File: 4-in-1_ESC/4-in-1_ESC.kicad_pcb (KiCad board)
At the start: 2 copper layers, 223 parts, among them CN1 SM10B-SRSS-TB, CN2 SM07B-SRSS-TB, Q1 BSC070N10NS3G, Q10 BSC070N10NS3G, Q11 BSC070N10NS3G, Q12 BSC070N10NS3G, Q13 BSC070N10NS3G, Q14 BSC070N10NS3G, Q15 BSC070N10NS3G, Q16 BSC070N10NS3G, Q17 BSC070N10NS3G, Q18 BSC070N10NS3G, Q19 BSC070N10NS3G, Q2 BSC070N10NS3G, Q20 BSC070N10NS3G, Q21 BSC070N10NS3G, Q22 BSC070N10NS3G, Q23 BSC070N10NS3G, Q24 BSC070N10NS3G, Q3 BSC070N10NS3G, Q4 BSC070N10NS3G, Q5 BSC070N10NS3G, Q6 BSC070N10NS3G, Q7 BSC070N10NS3G, Q8 BSC070N10NS3G, Q9 BSC070N10NS3G, U1 INA181A2IDBVR, U10 LMR51610XDBVR, U11 AMS1117-3.3_C347222, U12 STM32G071GBU6, U13 STM32G071GBU6, U2 JSM6288Q, U3 JSM6288Q, U4 JSM6288Q, U5 JSM6288Q, U6 STM32G071GBU6, U7 STM32G071GBU6

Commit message: update
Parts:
- removed C25: 100nF, Capacitor_SMD:C_0402_1005Metric
- removed R10, R13, R25, R28, R31, R43, R46, R7: 130k, Resistor_SMD:R_0402_1005Metric
- removed R12, R15, R27, R30, R33, R9: 1k, Resistor_SMD:R_0402_1005Metric
- added C82: 10nF, Capacitor_SMD:C_0201_0603Metric, F.Cu at (76.5, 44.4)
- added C86: 10nF, Capacitor_SMD:C_0201_0603Metric, F.Cu at (76.5, 46.2)
- added D13: XL-0201UGC, LED_SMD:LED_0201_0603Metric, F.Cu at (84.5, 78.6)
- added D14: XL-0201UGC, LED_SMD:LED_0201_0603Metric, F.Cu at (68.2, 122.1)
- added D15: XL-0201UGC, LED_SMD:LED_0201_0603Metric, F.Cu at (64.3, 78.6)
- added D16: XL-0201UGC, LED_SMD:LED_0201_0603Metric, F.Cu at (90.9, 63.0)
- added G***: LOGO, LOGO, F.Cu at (140.0, 105.9)
- added G***: LOGO, LOGO, F.Cu at (147.5, 81.7)
- added H4: MountingHole_Pad, MountingHole:MountingHole_3.2mm_M3_DIN965_Pad_TopBottom, F.Cu at (162.8, 81.7)
- added H5: MountingHole_Pad, MountingHole:MountingHole_3.2mm_M3_DIN965_Pad_TopBottom, F.Cu at (132.2, 81.7)
- added H6: MountingHole_Pad, MountingHole:MountingHole_3.2mm_M3_DIN965_Pad_TopBottom, F.Cu at (162.8, 112.2)
- added H7: MountingHole_Pad, MountingHole:MountingHole_3.2mm_M3_DIN965_Pad_TopBottom, F.Cu at (132.2, 112.2)
- added J1: BLDC Solder Pads, easyeda_import:3_Phase_Solder_Pads, F.Cu at (130.0, 88.4)
- added J2: BLDC Solder Pads, easyeda_import:3_Phase_Solder_Pads, F.Cu at (130.0, 105.3)
- added J3: BLDC Solder Pads, easyeda_import:3_Phase_Solder_Pads, F.Cu at (164.8, 89.8)
- added J4: BLDC Solder Pads, easyeda_import:3_Phase_Solder_Pads, F.Cu at (164.8, 106.4)
- added R100: 100R, Resistor_SMD:R_0201_0603Metric, F.Cu at (78.9, 81.5)
- added R101: 100R, Resistor_SMD:R_0201_0603Metric, F.Cu at (62.6, 124.9)
- added R102: 100R, Resistor_SMD:R_0201_0603Metric, F.Cu at (58.7, 81.5)
- added R103: 100R, Resistor_SMD:R_0201_0603Metric, F.Cu at (85.3, 65.8)
- added R104: 10k, Resistor_SMD:R_0201_0603Metric, F.Cu at (78.9, 83.2)
- added R105: 10k, Resistor_SMD:R_0201_0603Metric, F.Cu at (62.6, 126.7)
- added R106: 10k, Resistor_SMD:R_0201_0603Metric, F.Cu at (58.7, 83.2)
- added R107: 10k, Resistor_SMD:R_0201_0603Metric, F.Cu at (85.3, 67.6)
- added R108: 470R, Resistor_SMD:R_0201_0603Metric, F.Cu at (144.4, 120.4)
- added R109: 470R, Resistor_SMD:R_0201_0603Metric, F.Cu at (147.2, 121.4)
- added R110: 470R, Resistor_SMD:R_0201_0603Metric, F.Cu at (150.0, 120.2)
- added R111: 470R, Resistor_SMD:R_0201_0603Metric, F.Cu at (145.5, 109.9)
- added R112: 470R, Resistor_SMD:R_0201_0603Metric, F.Cu at (148.5, 109.9)
- added R113: 470R, Resistor_SMD:R_0201_0603Metric, F.Cu at (149.5, 109.9)
- added R114: 470R, Resistor_SMD:R_0201_0603Metric, F.Cu at (146.5, 109.9)
- added R115: 470R, Resistor_SMD:R_0201_0603Metric, F.Cu at (147.5, 109.9)
- added R88: 10k, Resistor_SMD:R_0201_0603Metric, F.Cu at (24.2, 26.7)
- added R89: 10k, Resistor_SMD:R_0201_0603Metric, F.Cu at (24.2, 75.7)
- added R90: 10k, Resistor_SMD:R_0201_0603Metric, F.Cu at (41.0, 116.3)
- added R91: 10k, Resistor_SMD:R_0201_0603Metric, F.Cu at (66.0, 30.2)
- added R92: 10k, Resistor_SMD:R_0201_0603Metric, F.Cu at (24.2, 28.4)
- added R93: 10k, Resistor_SMD:R_0201_0603Metric, F.Cu at (24.2, 77.5)
- added R94: 110k, Resistor_SMD:R_0201_0603Metric, F.Cu at (24.2, 30.2)
- added R95: 110k, Resistor_SMD:R_0201_0603Metric, F.Cu at (24.2, 79.2)
- added R96: 110k, Resistor_SMD:R_0201_0603Metric, F.Cu at (41.0, 118.1)
- added R97: 110k, Resistor_SMD:R_0201_0603Metric, F.Cu at (66.0, 31.9)
- added R98: 110k, Resistor_SMD:R_0201_0603Metric, F.Cu at (24.2, 31.9)
- added R99: 110k, Resistor_SMD:R_0201_0603Metric, F.Cu at (24.2, 81.0)
- C26, C27, C28, C34, C35, C36, C42, C43, C44, C50, C51, C52: value 10nF -> 1nF; footprint Capacitor_SMD:C_0402_1005Metric -> Capacitor_SMD:C_0201_0603Metric
- C29, C30, C31, C32, C33, C37, C38, C39, C40, C41, C45, C46, C47, C48, C49, C53, C54, C55, C56, C58, C59, C60, C61, C62, C63, C64, C66, C67, C68, C69, C70, C71, C72, C73, C76, C77, C78, C79, C80, C81, C84, C85, C88, C89, C90: footprint Capacitor_SMD:C_0402_1005Metric -> Capacitor_SMD:C_0201_0603Metric
- C57, C65, C83, C87: value C_Small -> 1uF; footprint Capacitor_SMD:C_0402_1005Metric -> Capacitor_SMD:C_0201_0603Metric
- CN1, Q10, Q12, Q14, Q16, Q18, Q2, Q20, Q22, Q24, Q4, Q6, Q8: moved to B.Cu
- R11, R14, R16, R17, R18, R19, R20, R21, R26, R29, R32, R34, R35, R36, R37, R38, R39, R44, R47, R50, R52, R53, R54, R55, R56, R57, R62, R63, R66, R69, R71, R72, R73, R74, R75, R76, R8, R80, R83, R84, R85, R86: footprint Resistor_SMD:R_0402_1005Metric -> Resistor_SMD:R_0201_0603Metric
- R22, R23, R24, R40, R41, R42, R58, R59, R60, R77, R78, R79: value 4.7R -> 2.2R; footprint Resistor_SMD:R_0402_1005Metric -> Resistor_SMD:R_0201_0603Metric
- R45, R48, R51, R64, R67, R70: value 1k -> 110k; footprint Resistor_SMD:R_0402_1005Metric -> Resistor_SMD:R_0201_0603Metric
- R49, R61, R65, R68: value 130k -> 10k; footprint Resistor_SMD:R_0402_1005Metric -> Resistor_SMD:R_0201_0603Metric
- R82, R87: value 10R -> 10k; footprint Resistor_SMD:R_0402_1005Metric -> Resistor_SMD:R_0201_0603Metric
- moved C59 126.1 mm to (16.9, 84.5)
- moved C60 126.1 mm to (16.9, 86.2)
- moved C61 126.1 mm to (16.9, 88.0)
- moved C70 124.4 mm to (19.4, 77.5)
- moved C64 124.3 mm to (19.4, 75.7)
- moved C58 123.5 mm to (16.9, 82.7)
- moved C53 123.5 mm to (16.9, 81.0)
- moved C52 123.5 mm to (16.9, 79.2)
- moved C51 123.5 mm to (16.9, 77.5)
- moved C50 123.4 mm to (16.9, 75.7)
- moved C31 122.3 mm to (33.6, 121.6)
- moved C32 122.2 mm to (33.6, 123.3)
- moved C33 122.1 mm to (33.6, 125.1)
- moved R65 121.2 mm to (21.8, 38.9)
- moved C69 116.7 mm to (19.4, 28.4)
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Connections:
- C1 pad 2: GND_BAT -> GND
- C10 pad 2: GND_BAT -> GND
- C11 pad 2: GND_BAT -> GND
- C12 pad 2: GND_BAT -> GND
- C13 pad 2: GND_BAT -> GND
- C14 pad 2: GND_BAT -> GND
- C15 pad 2: GND_BAT -> GND
- C16 pad 2: GND_BAT -> GND
- C17 pad 2: GND_BAT -> GND
- C18 pad 2: GND_BAT -> GND
- C19 pad 2: GND_BAT -> GND
- C2 pad 2: GND_BAT -> GND
- C20 pad 2: GND_BAT -> GND
- C21 pad 2: GND_BAT -> GND
- C22 pad 2: GND_BAT -> GND
- C23 pad 2: GND_BAT -> GND
- C24 pad 2: GND_BAT -> GND
- C3 pad 2: GND_BAT -> GND
- C4 pad 2: GND_BAT -> GND
- C5 pad 2: GND_BAT -> GND
- C6 pad 2: GND_BAT -> GND
- C7 pad 2: GND_BAT -> GND
- C8 pad 2: GND_BAT -> GND
- C9 pad 2: GND_BAT -> GND
- R45 pad 1: /BLDC DRIVE2/A -> /BLDC DRIVE/BEMF.A
- R45 pad 2: /BLDC DRIVE2/BEMF.A -> /BLDC DRIVE/A
- R48 pad 1: /BLDC DRIVE2/B -> /BLDC DRIVE1/BEMF.A
- R48 pad 2: /BLDC DRIVE2/BEMF.B -> /BLDC DRIVE1/A
- R49 pad 1: /BLDC DRIVE2/BEMF.C -> /BLDC DRIVE/BEMF.A
- R49 pad 2: /BLDC DRIVE2/BEMF.COMMON -> /BLDC DRIVE/BEMF.COMMON
- R51 pad 1: /BLDC DRIVE2/C -> /BLDC DRIVE2/BEMF.A
- R51 pad 2: /BLDC DRIVE2/BEMF.C -> /BLDC DRIVE2/A
- R61 pad 1: /BLDC DRIVE3/BEMF.A -> /BLDC DRIVE1/BEMF.A
- R61 pad 2: /BLDC DRIVE3/BEMF.COMMON -> /BLDC DRIVE1/BEMF.COMMON
- R64 pad 1: /BLDC DRIVE3/A -> /BLDC DRIVE3/BEMF.A
- R64 pad 2: /BLDC DRIVE3/BEMF.A -> /BLDC DRIVE3/A
- R65 pad 1: /BLDC DRIVE3/BEMF.B -> /BLDC DRIVE2/BEMF.A
- R65 pad 2: /BLDC DRIVE3/BEMF.COMMON -> /BLDC DRIVE2/BEMF.COMMON
- R67 pad 1: /BLDC DRIVE3/B -> /BLDC DRIVE/BEMF.B
- R67 pad 2: /BLDC DRIVE3/BEMF.B -> /BLDC DRIVE/B
- R68 pad 1: /BLDC DRIVE3/BEMF.C -> /BLDC DRIVE3/BEMF.A
- R70 pad 1: /BLDC DRIVE3/C -> /BLDC DRIVE1/BEMF.B
- R70 pad 2: /BLDC DRIVE3/BEMF.C -> /BLDC DRIVE1/B
- R82 pad 1: VBAT -> /BLDC DRIVE/BEMF.B
- R82 pad 2: Net-(U1-IN+) -> /BLDC DRIVE/BEMF.COMMON
- R87 pad 1: VBAT_IN -> /BLDC DRIVE1/BEMF.B
- R87 pad 2: Net-(U1-IN-) -> /BLDC DRIVE1/BEMF.COMMON
- U1 pad 3: Net-(U1-IN+) -> VBAT
- U1 pad 4: Net-(U1-IN-) -> VBAT_IN
- U12 pad 10: /BLDC DRIVE1/BEMF.A -> /STM32F051K8U7/NTC_TEMP
- U12 pad 11: /BLDC DRIVE1/BEMF.B -> /STM32F051K8U7/CURRENT_SENSE
- U12 pad 12: /BLDC DRIVE1/BEMF.C -> unconnected-(U12-PA6-Pad12)
- U12 pad 17: unconnected-(U12-PC6-Pad17) -> /STM32F051K8U7/LED_INDICATOR
- U12 pad 23: unconnected-(U12-PB3-Pad23) -> /BLDC DRIVE1/BEMF.B
- U12 pad 24: unconnected-(U12-PB4-Pad24) -> Net-(U12-PB4)
- U12 pad 26: /STM32F051K8U7/KISS_TELEM -> Net-(U12-PB6)
- U12 pad 27: /STM32F051K8U7/CURRENT_SENSE -> /BLDC DRIVE1/BEMF.A
- U12 pad 8: /DSHOT_M3 -> /BLDC DRIVE1/BEMF.C
- U13 pad 10: /BLDC DRIVE3/BEMF.A -> /STM32F051K8U9/NTC_TEMP
- U13 pad 11: /BLDC DRIVE3/BEMF.B -> /STM32F051K8U9/CURRENT_SENSE
- U13 pad 12: /BLDC DRIVE3/BEMF.C -> unconnected-(U13-PA6-Pad12)
- U13 pad 16: /STM32F051K8U9/HIN1 -> /BLDC DRIVE3/HIN1
- U13 pad 17: unconnected-(U13-PC6-Pad17) -> /STM32F051K8U9/LED_INDICATOR
- U13 pad 18: /STM32F051K8U9/HIN2 -> /BLDC DRIVE3/HIN2
- U13 pad 19: /STM32F051K8U9/HIN3 -> /BLDC DRIVE3/HIN3
- U13 pad 23: unconnected-(U13-PB3-Pad23) -> /BLDC DRIVE3/BEMF.B
- U13 pad 24: unconnected-(U13-PB4-Pad24) -> Net-(U13-PB4)
- U13 pad 26: /STM32F051K8U9/KISS_TELEM -> Net-(U13-PB6)
- U13 pad 27: /STM32F051K8U9/CURRENT_SENSE -> /BLDC DRIVE3/BEMF.A
- U13 pad 8: /DSHOT_M2 -> /BLDC DRIVE3/BEMF.C
- U2 pad 6: GND_BAT -> GND
- U3 pad 6: GND_BAT -> GND
- U4 pad 6: GND_BAT -> GND
- U5 pad 6: GND_BAT -> GND
- U6 pad 10: /BLDC DRIVE/BEMF.A -> /STM32F051K8U6/NTC_TEMP
- U6 pad 11: /BLDC DRIVE/BEMF.B -> /STM32F051K8U6/CURRENT_SENSE
- U6 pad 12: /BLDC DRIVE/BEMF.C -> unconnected-(U6-PA6-Pad12)
- U6 pad 17: unconnected-(U6-PC6-Pad17) -> /STM32F051K8U6/LED_INDICATOR
- U6 pad 23: unconnected-(U6-PB3-Pad23) -> /BLDC DRIVE/BEMF.B
- U6 pad 24: unconnected-(U6-PB4-Pad24) -> Net-(U6-PB4)
- U6 pad 26: /STM32F051K8U6/KISS_TELEM -> Net-(U6-PB6)
- U6 pad 27: /STM32F051K8U6/CURRENT_SENSE -> /BLDC DRIVE/BEMF.A
- U6 pad 8: /DSHOT_M4 -> /BLDC DRIVE/BEMF.C
- U7 pad 10: /BLDC DRIVE2/BEMF.A -> /STM32F051K8U8/NTC_TEMP
- U7 pad 11: /BLDC DRIVE2/BEMF.B -> /CURRENT_SENSE
- U7 pad 12: /BLDC DRIVE2/BEMF.C -> unconnected-(U7-PA6-Pad12)
- U7 pad 17: unconnected-(U7-PC6-Pad17) -> /STM32F051K8U8/LED_INDICATOR
- U7 pad 23: unconnected-(U7-PB3-Pad23) -> /BLDC DRIVE2/BEMF.B
- U7 pad 24: unconnected-(U7-PB4-Pad24) -> Net-(U7-PB4)
- U7 pad 26: /KISS_TELEM -> Net-(U7-PB6)
- U7 pad 27: /CURRENT_SENSE -> /BLDC DRIVE2/BEMF.A
- U7 pad 8: /DSHOT_M1 -> /BLDC DRIVE2/BEMF.C
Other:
- board outline added: 40 x 40 mm
- copper layers 2 -> 6

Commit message: changes
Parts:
- removed R108, R109, R110, R111, R112, R113, R114, R115: 470R, Resistor_SMD:R_0201_0603Metric
- removed U11: AMS1117-3.3_C347222, easyeda_import:SOT-223-4_L6.5-W3.5-P2.30-LS7.0-BR
- added J5: ~, easyeda_import:VBAT_SOLDER_PADS, F.Cu at (147.5, 82.5)
- added R116: 470R, Resistor_SMD:R_0201_0603Metric, F.Cu at (146.5, 110.0)
- added R117: 470R, Resistor_SMD:R_0201_0603Metric, F.Cu at (147.5, 110.0)
- added R118: 470R, Resistor_SMD:R_0201_0603Metric, F.Cu at (148.5, 110.0)
- added R119: 470R, Resistor_SMD:R_0201_0603Metric, F.Cu at (149.5, 110.0)
- added R120: 470R, Resistor_SMD:R_0201_0603Metric, F.Cu at (144.5, 127.3)
- added U8: TLV76733DRVR, easyeda_import:WSON-6_L2.0-W2.0-P0.65-TL-EP, F.Cu at (145.7, 105.9)
- H4, H5, H6, H7: footprint MountingHole:MountingHole_3.2mm_M3_DIN965_Pad_TopBottom -> easyeda_import:MountingHole_3.2mm_Custom
- J1, J2: footprint easyeda_import:3_Phase_Solder_Pads -> easyeda_import:3_Phase_Solder_Pads_Left
- J3, J4: footprint easyeda_import:3_Phase_Solder_Pads -> easyeda_import:3_Phase_Solder_Pads_Right
- moved C2 166.3 mm to (10.6, 15.0), turned to 0 degrees
- moved C12 160.5 mm to (10.6, 18.0)
- moved C22 159.6 mm to (10.6, 30.1), turned to 0 degrees
- moved C20 158.3 mm to (10.6, 24.0)
- moved C21 151.3 mm to (10.6, 27.0), turned to 0 degrees
- moved C15 149.2 mm to (10.6, 21.0)
- moved C61 85.4 mm to (96.2, 56.1), turned to -90 degrees
- moved C60 83.3 mm to (95.2, 57.9), turned to -90 degrees
- moved R74 80.3 mm to (97.6, 52.6), turned to 180 degrees
- moved C70 79.0 mm to (95.4, 56.1), turned to -90 degrees
- moved R73 77.6 mm to (94.1, 49.1), turned to -90 degrees
- moved C64 77.2 mm to (94.5, 57.9), turned to -90 degrees
- moved FB12 67.0 mm to (94.5, 56.1), turned to 90 degrees
- moved U5 65.2 mm to (94.2, 52.6), turned to 90 degrees
- moved C76 42.0 mm to (151.5, 104.9)
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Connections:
- CN2 pad 2: /KISS_TELEM -> Net-(CN2-Pad2)
- CN2 pad 3: /DSHOT_M1 -> Net-(CN2-Pad3)
- CN2 pad 4: /DSHOT_M2 -> Net-(CN2-Pad4)
- CN2 pad 5: /DSHOT_M3 -> Net-(CN2-Pad5)
- CN2 pad 6: /DSHOT_M4 -> Net-(CN2-Pad6)
- U12 pad 24: Net-(U12-PB4) -> /DSHOT_M3
- U12 pad 26: Net-(U12-PB6) -> /KISS_TELEM
- U13 pad 24: Net-(U13-PB4) -> /DSHOT_M2
- U13 pad 26: Net-(U13-PB6) -> /KISS_TELEM
- U6 pad 24: Net-(U6-PB4) -> /DSHOT_M4
- U6 pad 26: Net-(U6-PB6) -> /KISS_TELEM
- U7 pad 24: Net-(U7-PB4) -> /DSHOT_M1
- U7 pad 26: Net-(U7-PB6) -> /KISS_TELEM
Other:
- board size 40 x 40 mm -> 42.7 x 40.2 mm

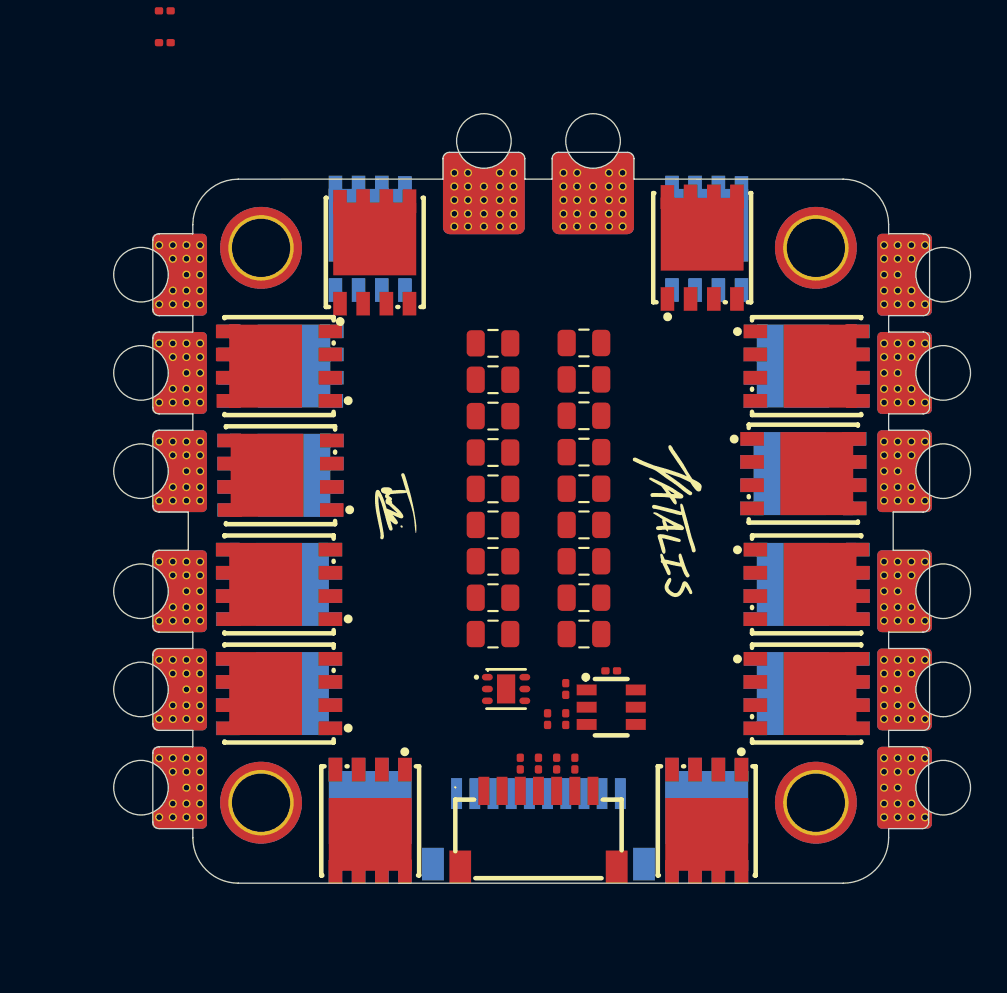
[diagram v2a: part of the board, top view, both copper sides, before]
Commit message: Schematic Updates
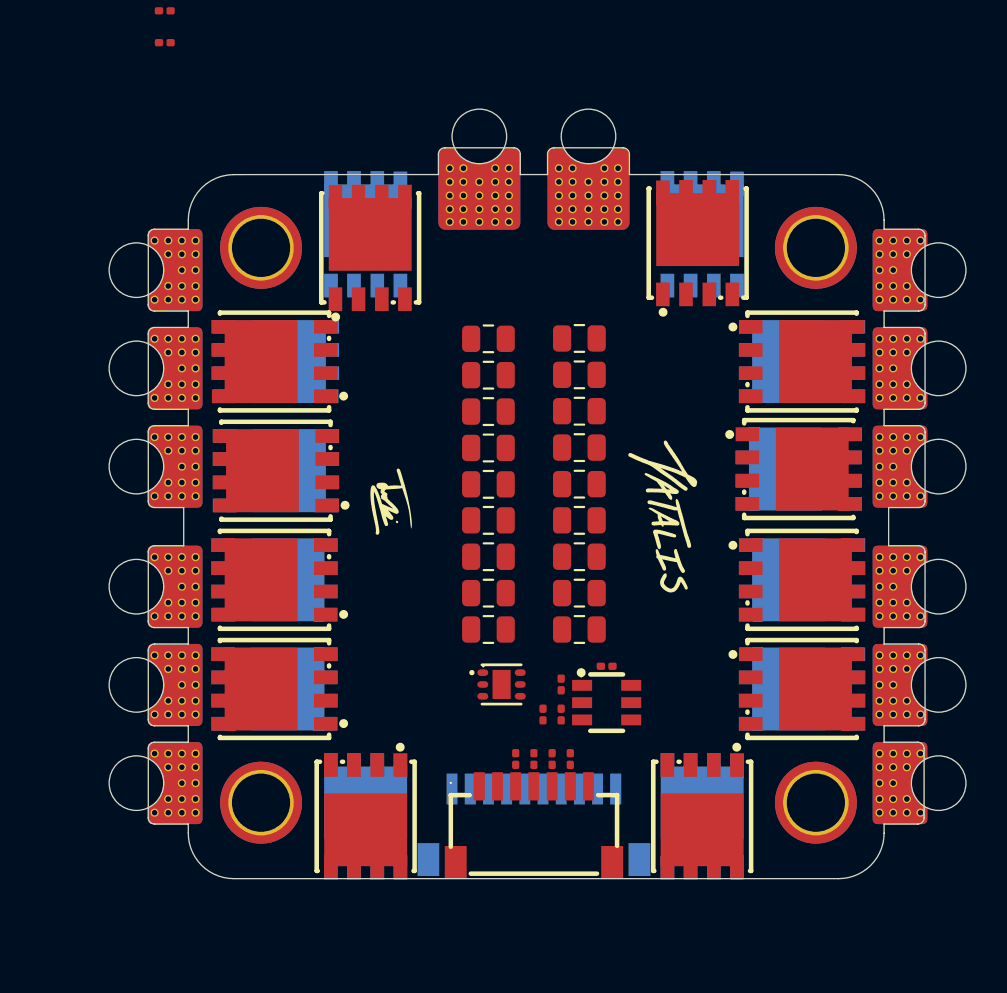
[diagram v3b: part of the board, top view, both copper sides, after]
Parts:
- moved C1 0.35 mm to (149.8, 94.6)
- moved C10 0.35 mm to (149.8, 102.6)
- moved C11 0.35 mm to (144.8, 90.7)
- moved C13 0.35 mm to (149.8, 86.6)
- moved C14 0.35 mm to (149.8, 96.6)
- moved C16 0.35 mm to (144.8, 98.6)
- moved C17 0.35 mm to (149.8, 90.6)
- moved C18 0.35 mm to (149.8, 100.6)
- moved C19 0.35 mm to (144.8, 92.7)
- moved C23 0.35 mm to (144.8, 86.7)
- moved C24 0.35 mm to (144.8, 100.6)
- moved C3 0.35 mm to (144.8, 88.7)
- moved C4 0.35 mm to (144.8, 102.6)
- moved C5 0.35 mm to (149.8, 88.6)
- moved C6 0.35 mm to (149.8, 98.6)
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
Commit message: update
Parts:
- removed C1, C10, C11, C12, C13, C14, C15, C17, C18, C2, C3, C4, C5, C6, C7, C8, C9: 10uF, Capacitor_SMD:C_0805_2012Metric
- removed R41, R42, R59, R60, R78, R79: 2.2R, Resistor_SMD:R_0201_0603Metric
- added C25: 10uF, Capacitor_SMD:C_1210_3225Metric, F.Cu at (109.5, 115.0)
- added C91: 100nF, Capacitor_SMD:C_0201_0603Metric, F.Cu at (119.2, 114.3)
- added C92: 10uF, Capacitor_SMD:C_1210_3225Metric, F.Cu at (109.5, 123.5)
- added C93: 10uF, Capacitor_SMD:C_1210_3225Metric, F.Cu at (109.5, 127.8)
- added C94: 10uF, Capacitor_SMD:C_1210_3225Metric, F.Cu at (109.5, 132.0)
- added D17: SMAJ40A, Diode_SMD:D_SMA, F.Cu at (147.2, 82.9)
- added NT1: NetTie_2, NetTie:NetTie-2_SMD_Pad2.0mm, F.Cu at (121.5, 110.2)
- added R1: 0.2m 6W SHUNT, easyeda_import:RES-SMD_L6.3-W3.1-1, B.Cu at (147.2, 82.9)
- added R121: 10k, Resistor_SMD:R_0201_0603Metric, F.Cu at (119.2, 116.0)
- added R25: 4.7R, Resistor_SMD:R_0201_0603Metric, F.Cu at (75.4, 104.1)
- added R27: 4.7R, Resistor_SMD:R_0201_0603Metric, F.Cu at (98.1, 104.1)
- added R28: 4.7R, Resistor_SMD:R_0201_0603Metric, F.Cu at (90.5, 105.8)
- added R30: 4.7R, Resistor_SMD:R_0201_0603Metric, F.Cu at (83.0, 105.8)
- added R31: 4.7R, Resistor_SMD:R_0201_0603Metric, F.Cu at (75.4, 105.8)
- added R33: 4.7R, Resistor_SMD:R_0201_0603Metric, F.Cu at (98.1, 105.8)
- added TH1: 10k 3380k, Resistor_SMD:R_0402_1005Metric, F.Cu at (95.9, 96.1)
- added TH2: 10k 3380k, Resistor_SMD:R_0402_1005Metric, F.Cu at (95.9, 92.1)
- added TH3: 10k 3380k, Resistor_SMD:R_0402_1005Metric, F.Cu at (95.9, 88.1)
- added TH4: 10k 3380k, Resistor_SMD:R_0402_1005Metric, F.Cu at (95.9, 84.1)
- C16, C19, C20, C21, C22, C23, C24: footprint Capacitor_SMD:C_0805_2012Metric -> Capacitor_SMD:C_1210_3225Metric
- C29, C30, C31, C37, C38, C39, C45, C46, C47, C53, C58, C59: value 4.7uF -> 4.7uF 25V X5R; footprint Capacitor_SMD:C_0201_0603Metric -> Capacitor_SMD:C_01005_0402Metric
- C66: value 100nF -> 10uF; footprint Capacitor_SMD:C_0201_0603Metric -> Capacitor_SMD:C_1210_3225Metric
- C82, C86: value 10nF -> 100nF
- D1, D10, D11, D12, D2, D3, D4, D5, D6, D7, D8, D9: value DSF1D E1D -> CDSQC4148-HF; footprint Diode_SMD:D_SOD-123F -> Diode_SMD:D_0402_1005Metric
- R22, R23, R24, R40, R58, R77: value 2.2R -> 4.7R
- U1: value INA181A2IDBVR -> INA180A2IDBVR; footprint easyeda_import:SOT-23-6_L2.9-W1.6-P0.95-LS2.8-BL -> easyeda_import:SOT-23-5_L3.0-W1.7-P0.95-LS2.8-BL; moved to B.Cu
- moved C22 135.1 mm to (103.8, 127.8)
- moved C21 134.2 mm to (103.8, 123.5)
- moved C20 133.3 mm to (103.8, 119.3)
- moved C46 105.4 mm to (90.4, 109.2)
- moved C47 98.9 mm to (82.9, 109.2)
- moved D8 85.8 mm to (72.7, 104.2)
- moved C59 84.8 mm to (98.0, 109.2)
- moved D9 84.6 mm to (72.7, 106.2)
- moved C66 83.4 mm to (109.5, 119.3)
- moved C39 82.1 mm to (98.0, 107.5)
- moved C86 78.9 mm to (119.2, 112.5)
- moved U1 77.1 mm to (145.5, 86.2), turned to 90 degrees
- moved C38 75.7 mm to (75.3, 107.5)
- moved D5 74.1 mm to (80.3, 104.2)
- moved D6 72.7 mm to (80.3, 106.2)
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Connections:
- C31 pad 1: /BLDC DRIVE/BOOT3 -> /BLDC DRIVE1/BOOT2
- C31 pad 2: /BLDC DRIVE/C -> /BLDC DRIVE1/B
- C38 pad 1: /BLDC DRIVE1/BOOT2 -> /BLDC DRIVE2/BOOT2
- C38 pad 2: /BLDC DRIVE1/B -> /BLDC DRIVE2/B
- C39 pad 1: /BLDC DRIVE1/BOOT3 -> /BLDC DRIVE3/BOOT2
- C39 pad 2: /BLDC DRIVE1/C -> /BLDC DRIVE3/B
- C46 pad 1: /BLDC DRIVE2/BOOT2 -> /BLDC DRIVE/BOOT3
- C46 pad 2: /BLDC DRIVE2/B -> /BLDC DRIVE/C
- C47 pad 1: /BLDC DRIVE2/BOOT3 -> /BLDC DRIVE1/BOOT3
- C47 pad 2: /BLDC DRIVE2/C -> /BLDC DRIVE1/C
- C58 pad 1: /BLDC DRIVE3/BOOT2 -> /BLDC DRIVE2/BOOT3
- C58 pad 2: /BLDC DRIVE3/B -> /BLDC DRIVE2/C
- C66 pad 1: GND -> VBAT_IN
- C66 pad 2: +3V3 -> GND
- C82 pad 1: GND -> +3V3
- C82 pad 2: VBAT_IN -> GND
- C86 pad 1: GND -> /CURRENT_SENSE
- C86 pad 2: VBAT -> GND
- J5 pad 1: VBAT -> VBAT_IN
- J5 pad 2: GND -> Net-(J5--)
- R24 pad 1: Net-(D3-A) -> Net-(D5-A)
- U1 pad 1: /CURRENT_SENSE -> Net-(U1-OUT)
- U1 pad 3: VBAT -> Net-(U1-IN+)
- U1 pad 4: VBAT_IN -> Net-(J5--)
- U1 pad 5: GND -> +3V3
- U12 pad 12: unconnected-(U12-PA6-Pad12) -> /STM32F051K8U7/VBAT_SENSE
- U13 pad 12: unconnected-(U13-PA6-Pad12) -> /STM32F051K8U9/VBAT_SENSE
- U6 pad 12: unconnected-(U6-PA6-Pad12) -> /STM32F051K8U6/VBAT_SENSE
- U7 pad 12: unconnected-(U7-PA6-Pad12) -> /VBAT_SENSE
